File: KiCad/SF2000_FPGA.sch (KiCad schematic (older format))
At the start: 7 parts, among them J3 Conn_02x03_Odd_Even, J4 Conn_02x01, U7 10M04SCE144

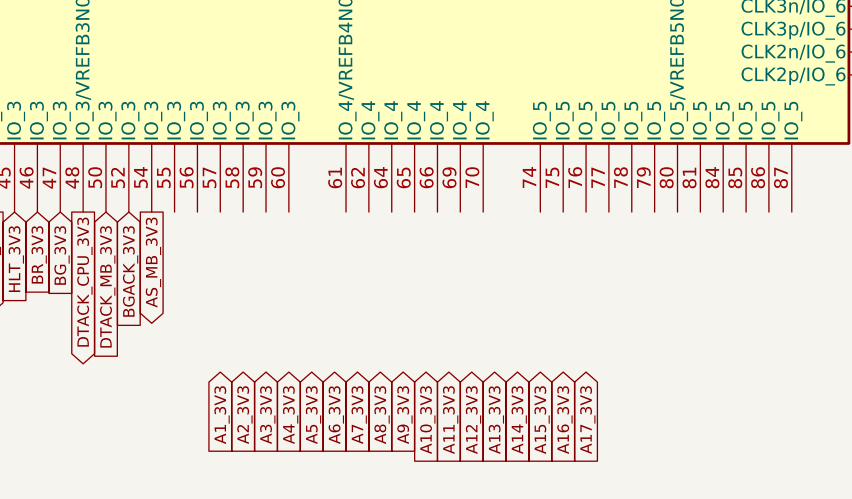
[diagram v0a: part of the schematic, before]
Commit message: Added SDIO-pinout and did more routing
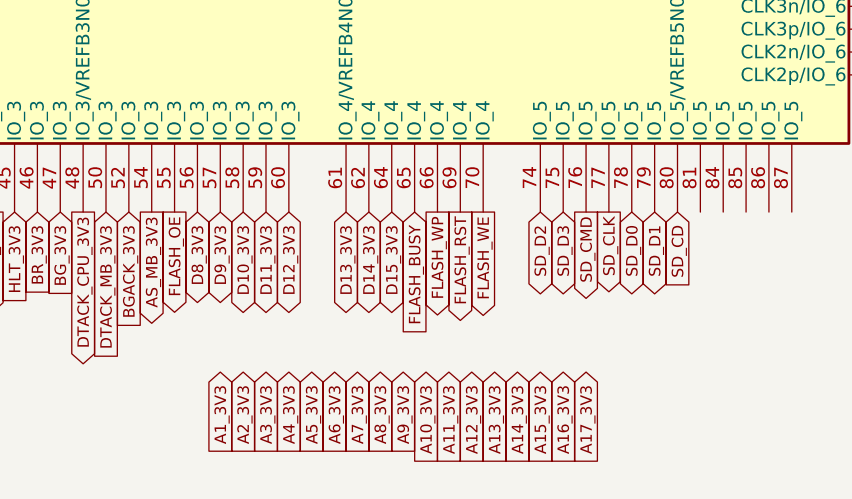
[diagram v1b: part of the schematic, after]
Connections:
- net FLASH_OE: now reaches U7.55 (IO_3)
- net D8_3V3: now reaches U7.56 (IO_3)
- net D9_3V3: now reaches U7.57 (IO_3)
- net D10_3V3: now reaches U7.58 (IO_3)
- net D11_3V3: now reaches U7.59 (IO_3)
- net D12_3V3: now reaches U7.60 (IO_3)
- net D13_3V3: now reaches U7.61 (IO_4/VREFB4N0)
- net D14_3V3: now reaches U7.62 (IO_4)
- net D15_3V3: now reaches U7.64 (IO_4)
- net FLASH_BUSY: now reaches U7.65 (IO_4)
- net FLASH_WP: now reaches U7.66 (IO_4)
- net FLASH_RST: now reaches U7.69 (IO_4)
- net FLASH_WE: now reaches U7.70 (IO_4)
- net SD_D2: now reaches U7.74 (IO_5)
- net SD_D3: now reaches U7.75 (IO_5)
- net SD_CMD: now reaches U7.76 (IO_5)
- net SD_CLK: now reaches U7.77 (IO_5)
- net SD_D0: now reaches U7.78 (IO_5)
- net SD_D1: now reaches U7.79 (IO_5)
- net SD_CD: now reaches U7.80 (IO_5/VREFB5N0)
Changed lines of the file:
@@
 Text GLabel 1350 2300 0    50   Output ~ 0
 VMA_3V3
+Text GLabel 3200 6000 3    50   BiDi ~ 0
+D9_3V3
+Text GLabel 3300 6000 3    50   BiDi ~ 0
+D10_3V3
+Text GLabel 3400 6000 3    50   BiDi ~ 0
+D11_3V3
+Text GLabel 3500 6000 3    50   BiDi ~ 0
+D12_3V3
+Text GLabel 3750 6000 3    50   BiDi ~ 0
+D13_3V3
+Text GLabel 3850 6000 3    50   BiDi ~ 0
+D14_3V3
+Text GLabel 3950 6000 3    50   BiDi ~ 0
+D15_3V3
+Text GLabel 3100 6000 3    50   BiDi ~ 0
+D8_3V3
+Text GLabel 3000 6000 3    50   Output ~ 0
+FLASH_OE
+Text GLabel 4350 6000 3    50   Output ~ 0
+FLASH_WE
+Text GLabel 4250 6000 3    50   Output ~ 0
+FLASH_RST
+Text GLabel 4150 6000 3    50   Output ~ 0
+FLASH_WP
+Text GLabel 4050 6000 3    50   Input ~ 0
+FLASH_BUSY
+Text GLabel 5000 6000 3    50   BiDi ~ 0
+SD_D0
+Text GLabel 5100 6000 3    50   BiDi ~ 0
+SD_D1
+Text GLabel 4600 6000 3    50   BiDi ~ 0
+SD_D2
+Text GLabel 4700 6000 3    50   BiDi ~ 0
+SD_D3
+Text GLabel 4800 6000 3    50   Output ~ 0
+SD_CMD
+Text GLabel 4900 6000 3    50   Output ~ 0
+SD_CLK
+Text GLabel 5200 6000 3    50   Input ~ 0
+SD_CD
 $EndSCHEMATC

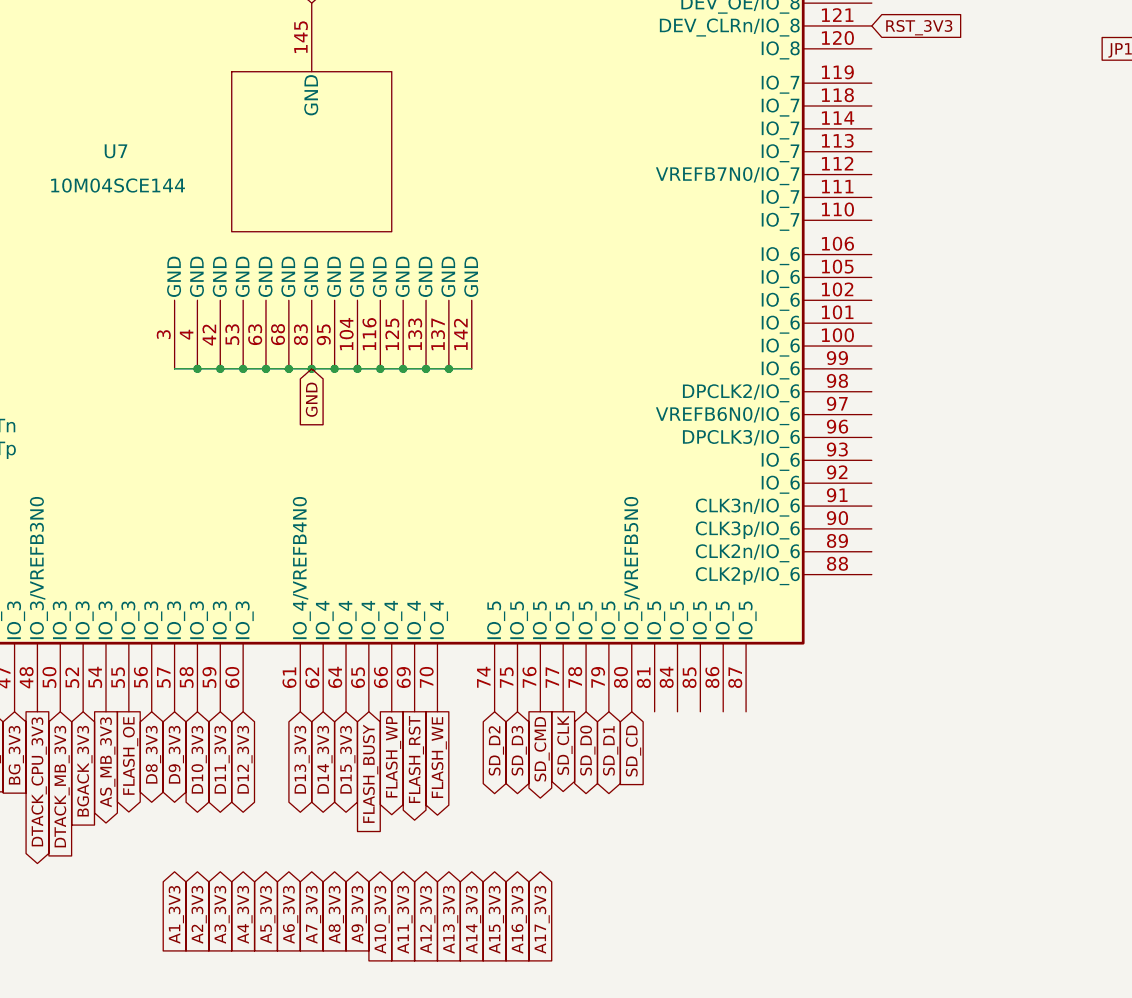
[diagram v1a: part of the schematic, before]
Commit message: added pull-ups for SDIO and did some more routing
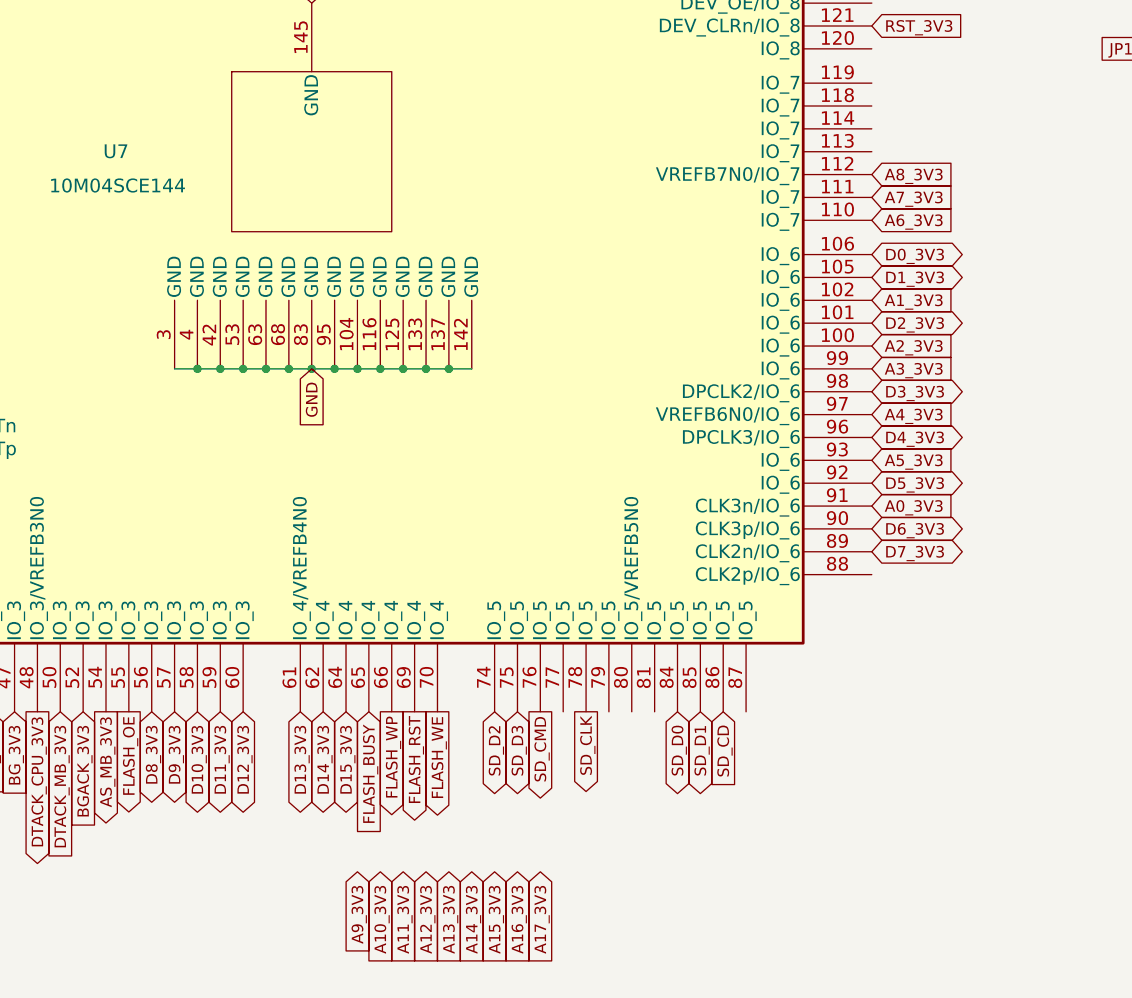
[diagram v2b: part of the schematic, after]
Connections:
- net A1_3V3: now also U7.102 (IO_6)
- net A2_3V3: now also U7.100 (IO_6)
- net A3_3V3: now also U7.99 (IO_6)
- net A4_3V3: now also U7.97 (VREFB6N0/IO_6)
- net A5_3V3: now also U7.93 (IO_6)
- net A6_3V3: now also U7.110 (IO_7)
- net A7_3V3: now also U7.111 (IO_7)
- net A8_3V3: now also U7.112 (VREFB7N0/IO_7)
- net SD_CD: now also U7.86 (IO_5); no longer U7.80 (IO_5/VREFB5N0)
- net SD_CLK: now also U7.78 (IO_5); no longer U7.77 (IO_5)
- net SD_D0: now also U7.84 (IO_5); no longer U7.78 (IO_5)
- net SD_D1: now also U7.85 (IO_5); no longer U7.79 (IO_5)
- net D2_3V3: now reaches U7.101 (IO_6)
- net D1_3V3: now reaches U7.105 (IO_6)
- net D0_3V3: now reaches U7.106 (IO_6)
- net D7_3V3: now reaches U7.89 (CLK2n/IO_6)
- net D6_3V3: now reaches U7.90 (CLK3p/IO_6)
- net A0_3V3: now reaches U7.91 (CLK3n/IO_6)
- net D5_3V3: now reaches U7.92 (IO_6)
- net D4_3V3: now reaches U7.96 (DPCLK3/IO_6)
- net D3_3V3: now reaches U7.98 (DPCLK2/IO_6)
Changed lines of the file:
@@
 Text GLabel 3300 1100 1    50   Input ~ 0
 3V3
-Text GLabel 3600 6700 3    50   Input ~ 0
-A5_3V3
-Text GLabel 3700 6700 3    50   Input ~ 0
-A6_3V3
 Text GLabel 1350 2800 0    50   Output ~ 0
 BOSS_3V3
 Text GLabel 1350 2900 0    50   Output ~ 0
 INT6_3V3
-Text GLabel 3500 6700 3    50   Input ~ 0
-A4_3V3
-Text GLabel 3400 6700 3    50   Input ~ 0
-A3_3V3
-Text GLabel 3800 6700 3    50   Input ~ 0
-A7_3V3
-Text GLabel 3900 6700 3    50   Input ~ 0
-A8_3V3
-Text GLabel 3300 6700 3    50   Input ~ 0
-A2_3V3
-Text GLabel 3200 6700 3    50   Input ~ 0
-A1_3V3
 Text GLabel 1350 4450 0    50   Input ~ 0
 FC0_3V3
@@
 Text GLabel 4050 6000 3    50   Input ~ 0
 FLASH_BUSY
-Text GLabel 5000 6000 3    50   BiDi ~ 0
+Text GLabel 5400 6000 3    50   BiDi ~ 0
 SD_D0
-Text GLabel 5100 6000 3    50   BiDi ~ 0
+Text GLabel 5500 6000 3    50   BiDi ~ 0
 SD_D1
 Text GLabel 4600 6000 3    50   BiDi ~ 0
@@
 Text GLabel 4800 6000 3    50   Output ~ 0
 SD_CMD
-Text GLabel 4900 6000 3    50   Output ~ 0
+Text GLabel 5000 6000 3    50   Output ~ 0
 SD_CLK
-Text GLabel 5200 6000 3    50   Input ~ 0
+Text GLabel 5600 6000 3    50   Input ~ 0
 SD_CD
+Text GLabel 6250 4000 2    50   BiDi ~ 0
+D0_3V3
+Text GLabel 6250 4100 2    50   BiDi ~ 0
+D1_3V3
+Text GLabel 6250 4300 2    50   BiDi ~ 0
+D2_3V3
+Text GLabel 6250 4600 2    50   BiDi ~ 0
+D3_3V3
+Text GLabel 6250 4800 2    50   BiDi ~ 0
+D4_3V3
+Text GLabel 6250 5000 2    50   BiDi ~ 0
+D5_3V3
+Text GLabel 6250 5200 2    50   BiDi ~ 0
+D6_3V3
+Text GLabel 6250 5300 2    50   BiDi ~ 0
+D7_3V3
+Text GLabel 6250 4900 2    50   Input ~ 0
+A5_3V3
+Text GLabel 6250 3850 2    50   Input ~ 0
+A6_3V3
+Text GLabel 6250 4700 2    50   Input ~ 0
+A4_3V3
+Text GLabel 6250 4500 2    50   Input ~ 0
+A3_3V3
+Text GLabel 6250 3750 2    50   Input ~ 0
+A7_3V3
+Text GLabel 6250 3650 2    50   Input ~ 0
+A8_3V3
+Text GLabel 6250 4400 2    50   Input ~ 0
+A2_3V3
+Text GLabel 6250 4200 2    50   Input ~ 0
+A1_3V3
+Text GLabel 6250 5100 2    50   Input ~ 0
+A0_3V3
 $EndSCHEMATC

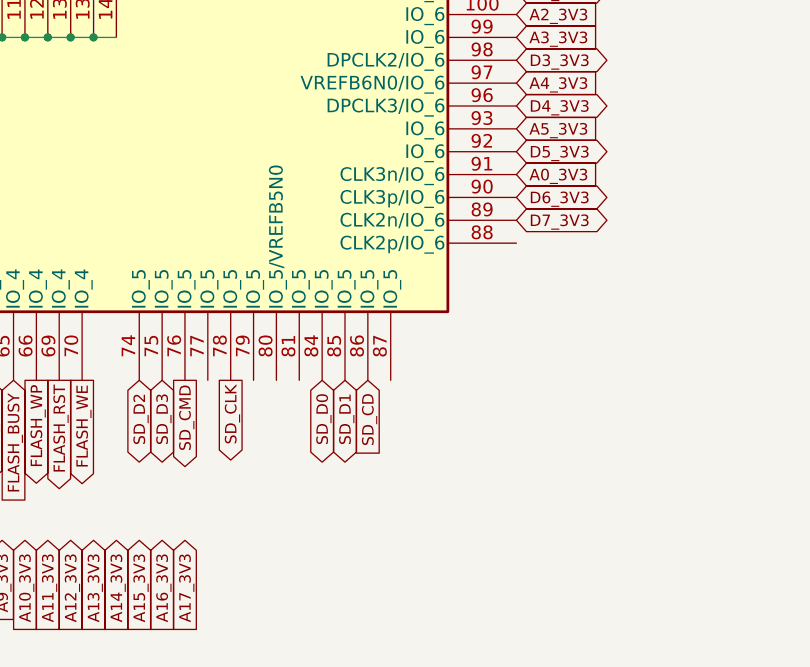
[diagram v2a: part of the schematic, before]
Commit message: more routing and pin assignments done to FPGA
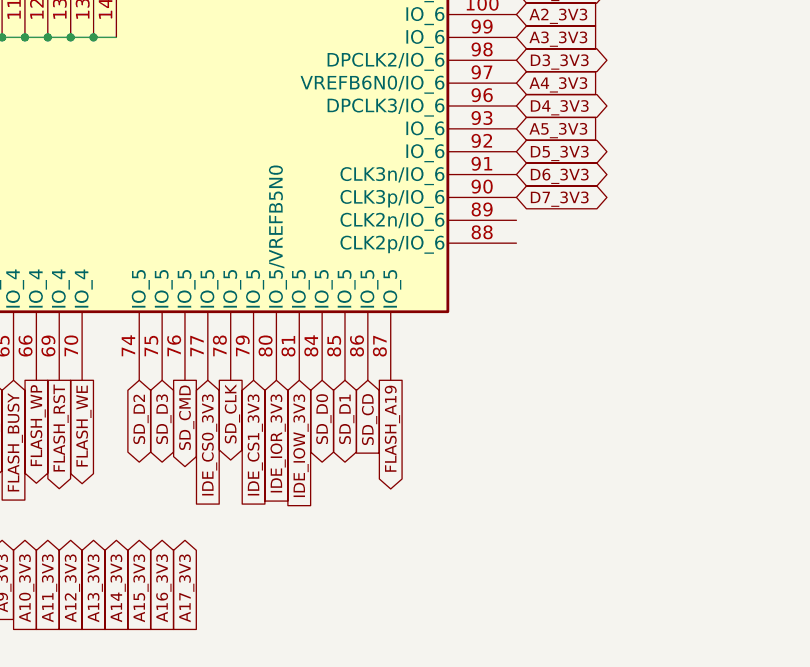
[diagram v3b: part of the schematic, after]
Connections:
- net A0_3V3 is gone; now on net D6_3V3: U7.91 (CLK3n/IO_6)
- net D6_3V3: no longer U7.90 (CLK3p/IO_6)
- net D7_3V3: now also U7.90 (CLK3p/IO_6); no longer U7.89 (CLK2n/IO_6)
- net IDE_CS0_3V3: now reaches U7.77 (IO_5)
- net IDE_CS1_3V3: now reaches U7.79 (IO_5)
- net IDE_IOR_3V3: now reaches U7.80 (IO_5/VREFB5N0)
- net IDE_IOW_3V3: now reaches U7.81 (IO_5)
- net FLASH_A19: now reaches U7.87 (IO_5)
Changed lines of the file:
@@
 Text GLabel 6250 5000 2    50   BiDi ~ 0
 D5_3V3
+Text GLabel 6250 5100 2    50   BiDi ~ 0
+D6_3V3
 Text GLabel 6250 5200 2    50   BiDi ~ 0
-D6_3V3
-Text GLabel 6250 5300 2    50   BiDi ~ 0
 D7_3V3
 Text GLabel 6250 4900 2    50   Input ~ 0
@@
 Text GLabel 6250 4200 2    50   Input ~ 0
 A1_3V3
-Text GLabel 6250 5100 2    50   Input ~ 0
-A0_3V3
+Text GLabel 5300 6000 3    50   Input ~ 0
+IDE_IOW_3V3
+Text GLabel 5200 6000 3    50   Input ~ 0
+IDE_IOR_3V3
+Text GLabel 5100 6000 3    50   Input ~ 0
+IDE_CS1_3V3
+Text GLabel 4900 6000 3    50   Input ~ 0
+IDE_CS0_3V3
+Text GLabel 5700 6000 3    50   Output ~ 0
+FLASH_A19
 $EndSCHEMATC

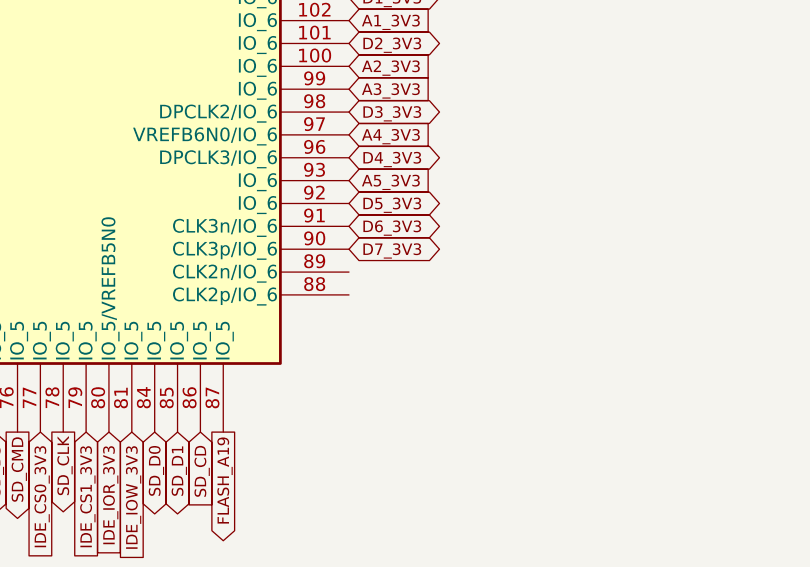
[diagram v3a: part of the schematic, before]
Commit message: added Oscillator, pull-up resistor and more routing done
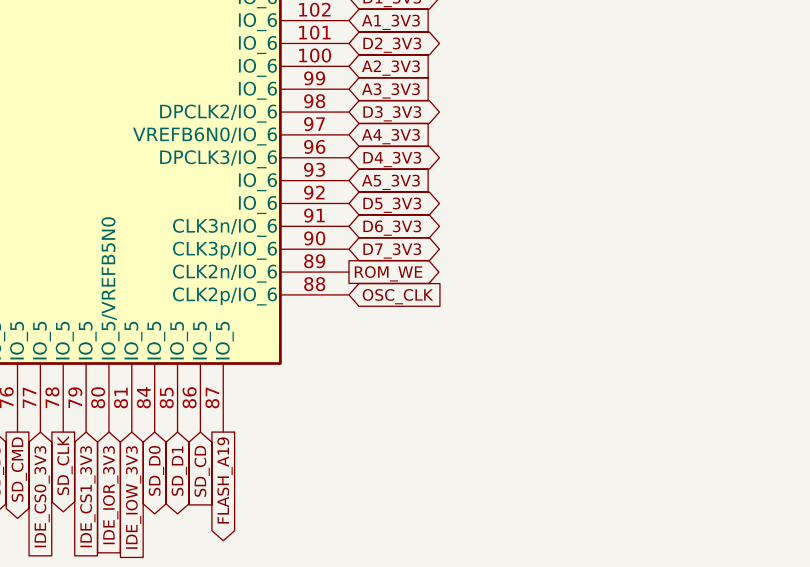
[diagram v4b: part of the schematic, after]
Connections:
- net OSC_CLK: now reaches U7.88 (CLK2p/IO_6)
- net ROM_WE: now reaches U7.89 (CLK2n/IO_6)
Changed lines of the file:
@@
 Text GLabel 5700 6000 3    50   Output ~ 0
 FLASH_A19
+Text GLabel 6250 5400 2    50   Input ~ 0
+OSC_CLK
+Text GLabel 6250 5300 2    50   Output ~ 0
+ROM_WE
 $EndSCHEMATC
